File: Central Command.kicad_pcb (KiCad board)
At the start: 4 copper layers, 50.8 x 50.8 mm, 50 parts, among them P101 CONN_01X10, P102 CONN_01X10, P103 CONN_01X04, P104 CONN_01X02, P105 CONN_01X04, P106 CONN_01X02, P201 CONN_01X06, P202 CONN_01X04, P203 CONN_01X04, P204 CONN_01X03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

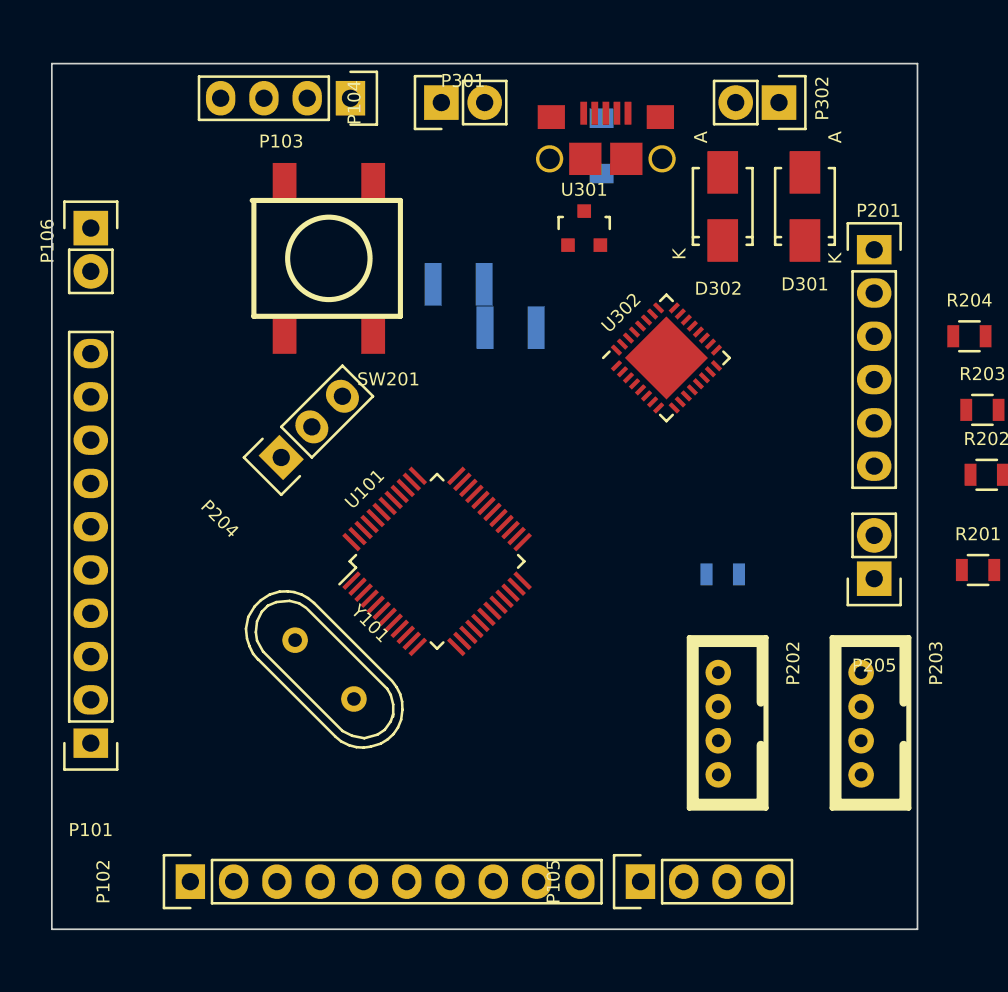
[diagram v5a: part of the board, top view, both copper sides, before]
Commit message: Added mounting holes (again?)
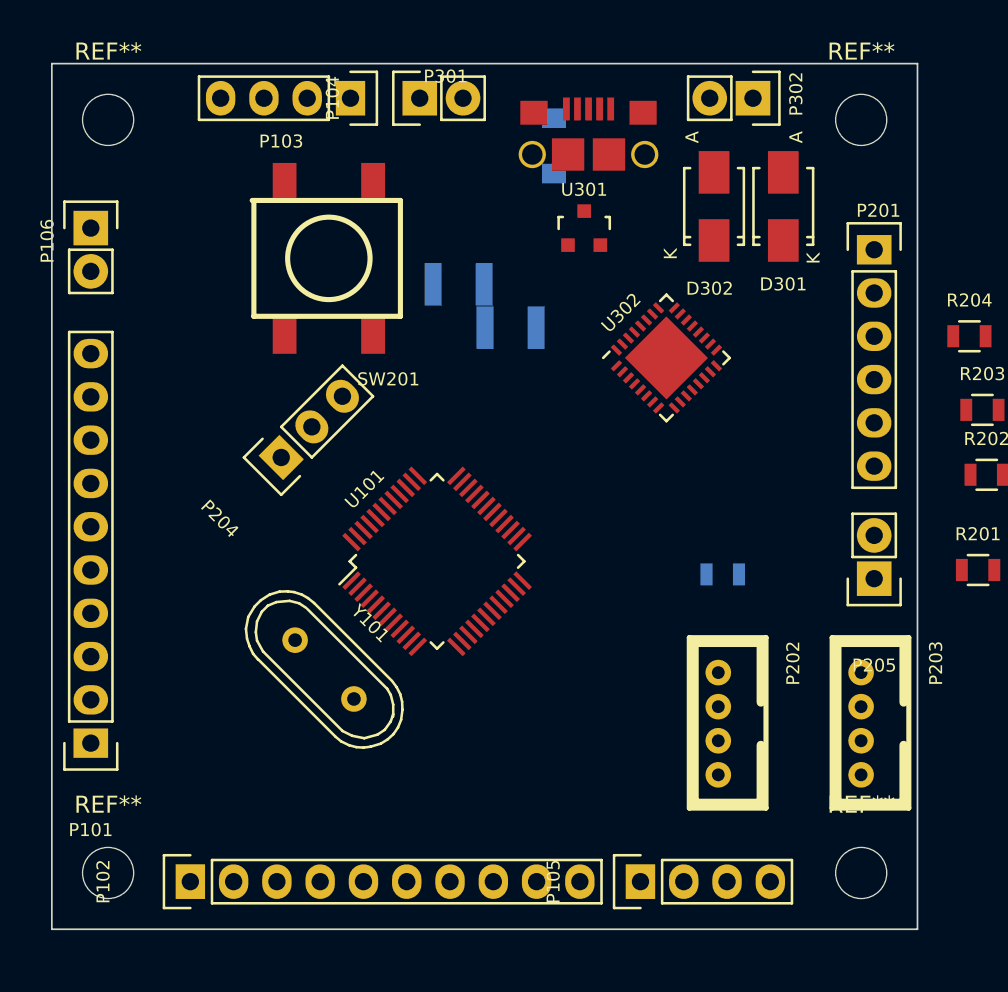
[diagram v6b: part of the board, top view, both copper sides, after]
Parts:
- added REF**: MountingHole_3mm, Mounting_Holes:MountingHole_3mm, F.Cu at (149.1, 123.7)
- added REF**: MountingHole_3mm, Mounting_Holes:MountingHole_3mm, F.Cu at (104.9, 123.7)
- added REF**: MountingHole_3mm, Mounting_Holes:MountingHole_3mm, F.Cu at (149.1, 79.5)
- added REF**: MountingHole_3mm, Mounting_Holes:MountingHole_3mm, F.Cu at (104.9, 79.5)
- moved L301 2.79 mm to (131.1, 81.0)
- moved P302 1.55 mm to (142.7, 78.2)
- moved P104 1.30 mm to (123.2, 78.2)
- moved D301 1.27 mm to (144.5, 84.6)
- moved P301 1.05 mm to (133.1, 81.5)
- moved D302 0.51 mm to (140.5, 84.6)
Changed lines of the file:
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@@
     (tracks 0)
     (zones 0)
-    (modules 50)
+    (modules 54)
     (nets 85)
   )
@@
     (add_net "Net-(U302-Pad9)")
   )
+  (module Mounting_Holes:MountingHole_3mm (layer F.Cu)
+    (at 149.098 123.698)
+    (descr "Mounting hole, Befestigungsbohrung, 3mm, No Annular, Kein Restring,")
+    (tags "Mounting hole, Befestigungsbohrung, 3mm, No Annular, Kein Restring,")
+    (fp_text reference REF** (at 0 -4.0005) (layer F.SilkS)
+      (effects (font (size 1 1) (thickness 0.15)))
+    )
+    (fp_text value MountingHole_3mm (at 1.00076 5.00126) (layer F.Fab) hide
+      (effects (font (size 1 1) (thickness 0.15)))
+    )
+    (fp_circle (center 0 0) (end 3 0) (layer Cmts.User) (width 0.381))
+    (pad 1 thru_hole circle (at 0 0) (size 3 3) (drill 3) (layers))
+  )
+  (module Mounting_Holes:MountingHole_3mm (layer F.Cu)
+    (at 104.902 123.698)
+    (descr "Mounting hole, Befestigungsbohrung, 3mm, No Annular, Kein Restring,")
+    (tags "Mounting hole, Befestigungsbohrung, 3mm, No Annular, Kein Restring,")
+    (fp_text reference REF** (at 0 -4.0005) (layer F.SilkS)
+      (effects (font (size 1 1) (thickness 0.15)))
+    )
+    (fp_text value MountingHole_3mm (at 1.00076 5.00126) (layer F.Fab) hide
+      (effects (font (size 1 1) (thickness 0.15)))
+    )
+    (fp_circle (center 0 0) (end 3 0) (layer Cmts.User) (width 0.381))
+    (pad 1 thru_hole circle (at 0 0) (size 3 3) (drill 3) (layers))
+  )
+  (module Mounting_Holes:MountingHole_3mm (layer F.Cu)
+    (at 149.098 79.502)
+    (descr "Mounting hole, Befestigungsbohrung, 3mm, No Annular, Kein Restring,")
+    (tags "Mounting hole, Befestigungsbohrung, 3mm, No Annular, Kein Restring,")
+    (fp_text reference REF** (at 0 -4.0005) (layer F.SilkS)
+      (effects (font (size 1 1) (thickness 0.15)))
+    )
+    (fp_text value MountingHole_3mm (at 1.00076 5.00126) (layer F.Fab) hide
+      (effects (font (size 1 1) (thickness 0.15)))
+    )
+    (fp_circle (center 0 0) (end 3 0) (layer Cmts.User) (width 0.381))
+    (pad 1 thru_hole circle (at 0 0) (size 3 3) (drill 3) (layers))
+  )
   (module Capacitors_SMD:C_0805 (layer F.Cu)
     (at 192.923571 126.727)
@@
   )
   (module Diodes_SMD:Diode-SMA_Standard (layer F.Cu)
-    (at 145.796 84.582 90)
+    (at 144.526 84.582 90)
     (descr "Diode SMA")
     (tags "Diode SMA")
@@
       (effects (font (size 0.762 0.762) (thickness 0.127)))
     )
-    (fp_text user A (at 4.064 1.778 90) (layer F.SilkS)
+    (fp_text user A (at 4.064 0.762 90) (layer F.SilkS)
       (effects (font (size 0.762 0.762) (thickness 0.127)))
     )
@@
   )
   (module Diodes_SMD:Diode-SMA_Standard (layer F.Cu)
-    (at 140.97 84.582 90)
+    (at 140.462 84.582 90)
     (descr "Diode SMA")
     (tags "Diode SMA")
@@
   )
   (module Inductors_NEOSID:Neosid_Inductor_SM1206 (layer B.Cu)
-    (at 133.858 81.026 270)
+    (at 131.064 81.026 270)
     (descr "Neosid, Inductor, SM1206, Festinduktivitaet, SMD,")
     (tags "Neosid, Inductor, SM1206, Festinduktivitaet, SMD,")
@@
   )
   (module Pin_Headers:Pin_Header_Straight_1x02 (layer F.Cu)
-    (at 124.46 78.486 90)
+    (at 123.19 78.232 90)
     (descr "Through hole pin header")
     (tags "pin header")
@@
   )
   (module Pin_Headers:Pin_Header_Straight_1x02 (layer F.Cu)
-    (at 144.272 78.486 270)
+    (at 142.748 78.232 270)
     (descr "Through hole pin header")
     (tags "pin header")
@@
   )
   (module CentralCommand:10118193 (layer F.Cu)
-    (at 134.112 81.788)
+    (at 133.096 81.534)
     (fp_text reference P301 (at -8.382 -4.572) (layer F.SilkS)
       (effects (font (size 0.762 0.762) (thickness 0.127)))
@@
       (net 1 GND))
   )
+  (module Mounting_Holes:MountingHole_3mm (layer F.Cu)
+    (at 104.902 79.502)
+    (descr "Mounting hole, Befestigungsbohrung, 3mm, No Annular, Kein Restring,")
+    (tags "Mounting hole, Befestigungsbohrung, 3mm, No Annular, Kein Restring,")
+    (fp_text reference REF** (at 0 -4.0005) (layer F.SilkS)
+      (effects (font (size 1 1) (thickness 0.15)))
+    )
+    (fp_text value MountingHole_3mm (at 1.00076 5.00126) (layer F.Fab) hide
+      (effects (font (size 1 1) (thickness 0.15)))
+    )
+    (fp_circle (center 0 0) (end 3 0) (layer Cmts.User) (width 0.381))
+    (pad 1 thru_hole circle (at 0 0) (size 3 3) (drill 3) (layers))
+  )
   (gr_line (start 101.6 127) (end 101.6 76.2) (angle 90) (layer Edge.Cuts) (width 0.1))

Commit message: Finished laying out power section
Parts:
- C301, C302, C303, C304: moved to B.Cu
- moved C301 73.5 mm to (129.3, 77.9), turned to 180 degrees
- moved C302 67.7 mm to (133.7, 98.3), turned to 270 degrees
- moved C304 50.9 mm to (141.7, 99.1), turned to 270 degrees
- moved C303 39.5 mm to (138.0, 99.4)
- moved C306 10.2 mm to (133.6, 83.1), turned to 90 degrees
- moved R205 5.35 mm to (145.9, 108.2)
- moved C305 5.18 mm to (129.5, 86.6), turned to 270 degrees
- moved L301 4.37 mm to (134.6, 78.5), turned to 0 degrees
- moved U302 2.44 mm to (138.0, 95.9)
- moved R204 0.74 mm to (156.1, 92.6)
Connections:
- P301 pad 6: (no net) -> GND
- P301 pad 7: (no net) -> GND
- P301 pad 8: (no net) -> GND
- P301 pad 9: (no net) -> GND
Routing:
- net GND: track 0.00 -> 24.8 mm, vias 0 -> 6
- net Net-(C305-Pad1): track 0.00 -> 17.8 mm, vias 0 -> 1
- net Net-(C302-Pad1): track 0.00 -> 7.57 mm, vias 0 -> 1
- net Net-(D301-Pad2): track 0.00 -> 5.66 mm
- net Net-(C301-Pad1): track 0.00 -> 5.51 mm, vias 0 -> 1
- net /Comm/PWR: track 0.00 -> 5.40 mm, vias 0 -> 3

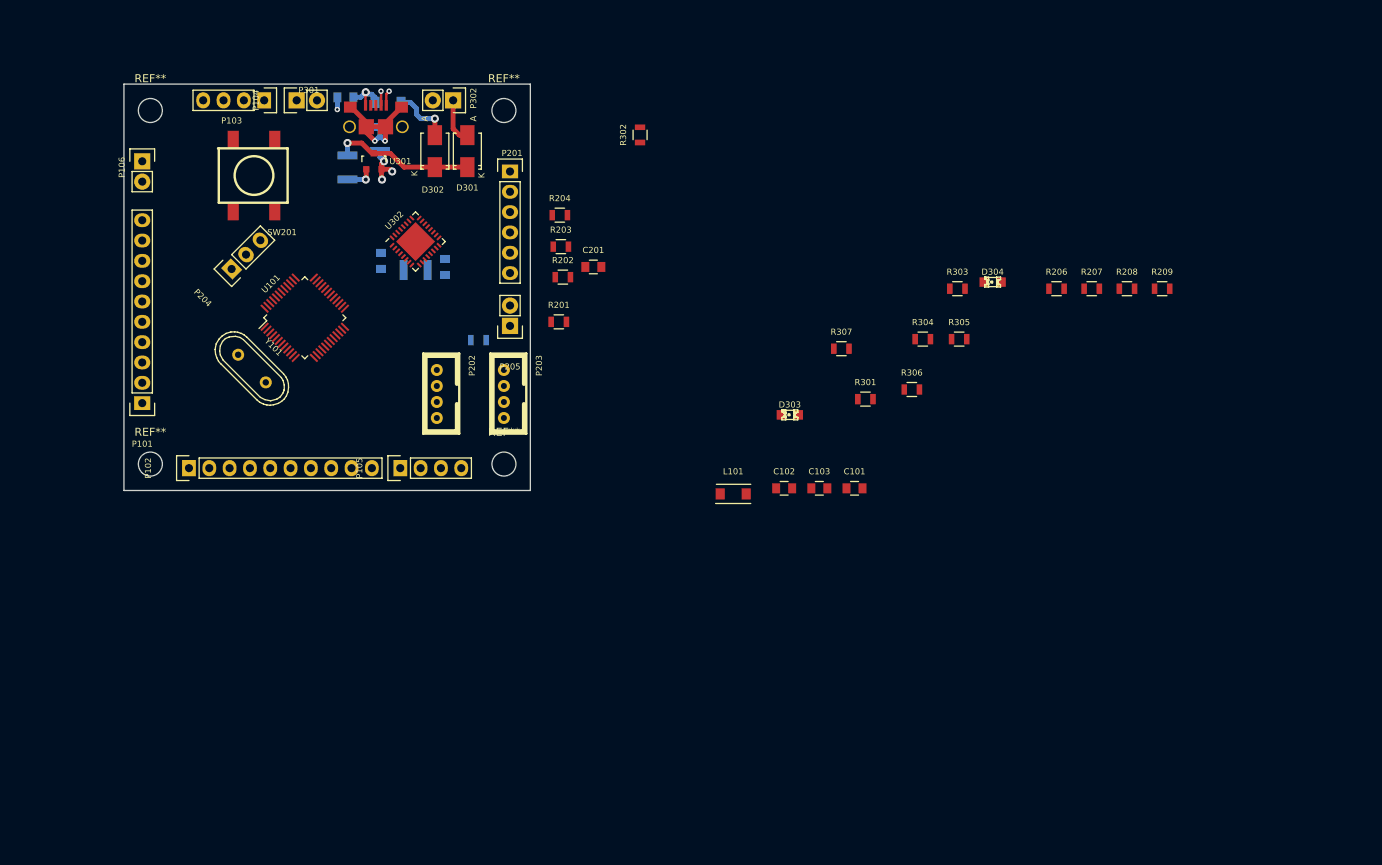
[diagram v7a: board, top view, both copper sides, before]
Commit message: Ripped up previous power layout and placed all FTDI components (finished page 3 of schematic)
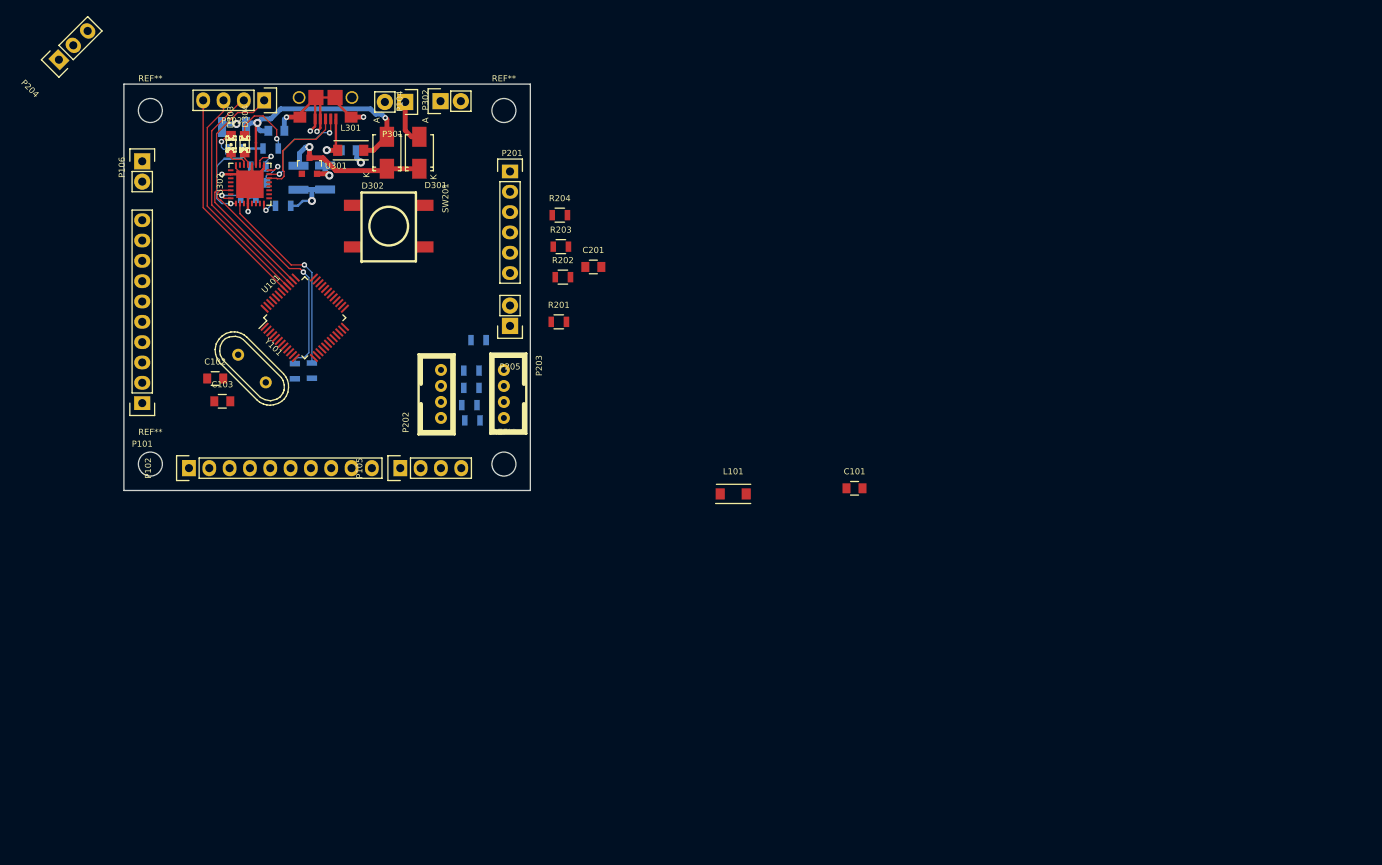
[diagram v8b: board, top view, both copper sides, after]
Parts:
- L301: moved to F.Cu
- R206, R207, R208, R209, R301, R302, R303, R304, R305, R306, R307: moved to B.Cu
- moved D304 95.1 mm to (116.7, 83.7), turned to 90 degrees
- moved R306 89.7 mm to (115.5, 84.4), turned to 180 degrees
- moved R209 87.8 mm to (145.2, 118.2)
- moved R305 86.1 mm to (121.5, 91.4), turned to 180 degrees
- moved R304 86.1 mm to (117.1, 90.4), turned to 180 degrees
- moved R208 83.5 mm to (144.8, 116.3)
- moved R303 81.3 mm to (125.1, 112.0), turned to 90 degrees
- moved R301 81.3 mm to (118.4, 86.5), turned to 180 degrees
- moved R207 78.5 mm to (145.0, 114.2)
- moved D303 77.6 mm to (115.0, 83.7), turned to 90 degrees
- moved R307 75.6 mm to (119.9, 84.3)
- moved C103 75.4 mm to (113.9, 115.8)
- moved R206 73.9 mm to (145.0, 112.0)
- moved C102 72.4 mm to (113.0, 113.0)
- moved R302 52.3 mm to (123.0, 112.1)
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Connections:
- net Net-(C302-Pad1) renamed /Power/VCCIO
- P301 pad 6: GND -> (no net)
- P301 pad 7: GND -> (no net)
- P301 pad 8: GND -> (no net)
- P301 pad 9: GND -> (no net)
- U302 pad 33: (no net) -> GND
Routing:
- net /Power/VCCIO: track 7.57 -> 46.2 mm, vias 1 -> 3
- net GND: track 24.8 -> 57.3 mm, vias 6 -> 9
- net /SPI1_NSS: track 0.00 -> 30.2 mm
- net Net-(R302-Pad2): track 0.00 -> 29.9 mm, vias 0 -> 1
- net /SPI1_SCK: track 0.00 -> 28.7 mm
- net /SPI1_MISO: track 0.00 -> 28.2 mm
- net /SPI1_MOSI: track 0.00 -> 27.8 mm
- net Net-(R303-Pad2): track 0.00 -> 24.6 mm, vias 0 -> 1
- net Net-(P301-Pad3): track 0.00 -> 13.6 mm
- net Net-(P301-Pad2): track 0.00 -> 13.0 mm, vias 0 -> 2
- net Net-(D304-Pad2): track 0.00 -> 8.94 mm, vias 0 -> 1
- net Net-(C304-Pad1): track 0.00 -> 4.06 mm, vias 0 -> 1
- net Net-(R304-Pad2): track 0.00 -> 3.77 mm, vias 0 -> 1
- net Net-(R301-Pad1): track 0.00 -> 3.72 mm, vias 0 -> 1
- net Net-(D303-Pad2): track 0.00 -> 3.12 mm, vias 0 -> 1
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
